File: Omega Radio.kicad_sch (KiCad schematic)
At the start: 14 parts, among them J1 AVR-ISP-6, SW1 Reset, U1 ATmega328P-P

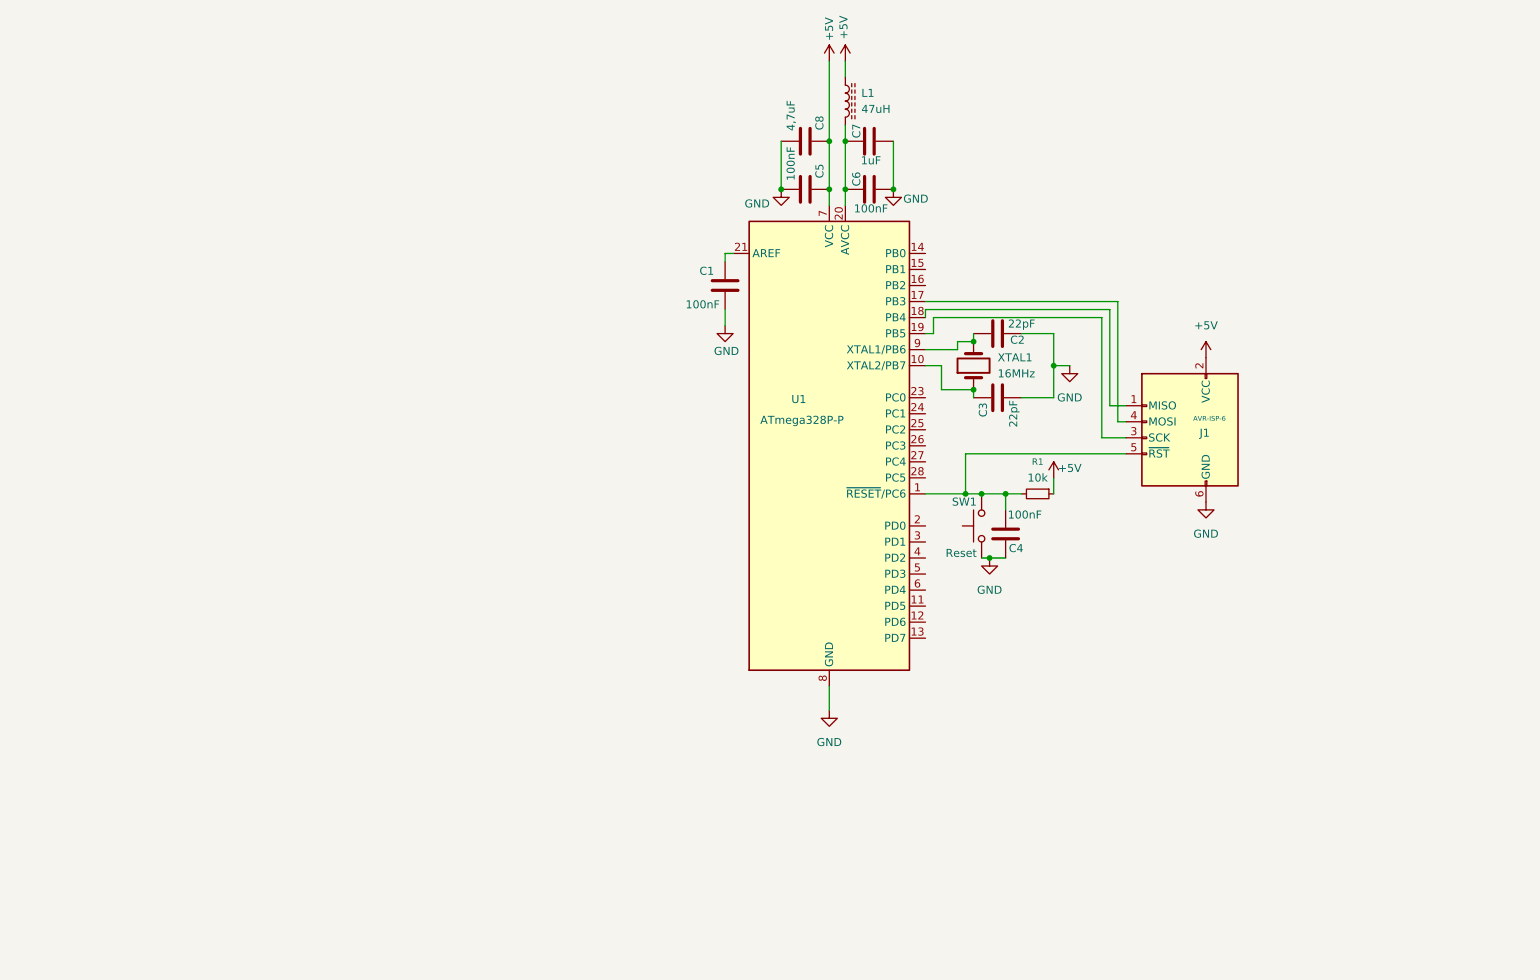
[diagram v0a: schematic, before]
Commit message: Introduction of the regulator to the microprocessor
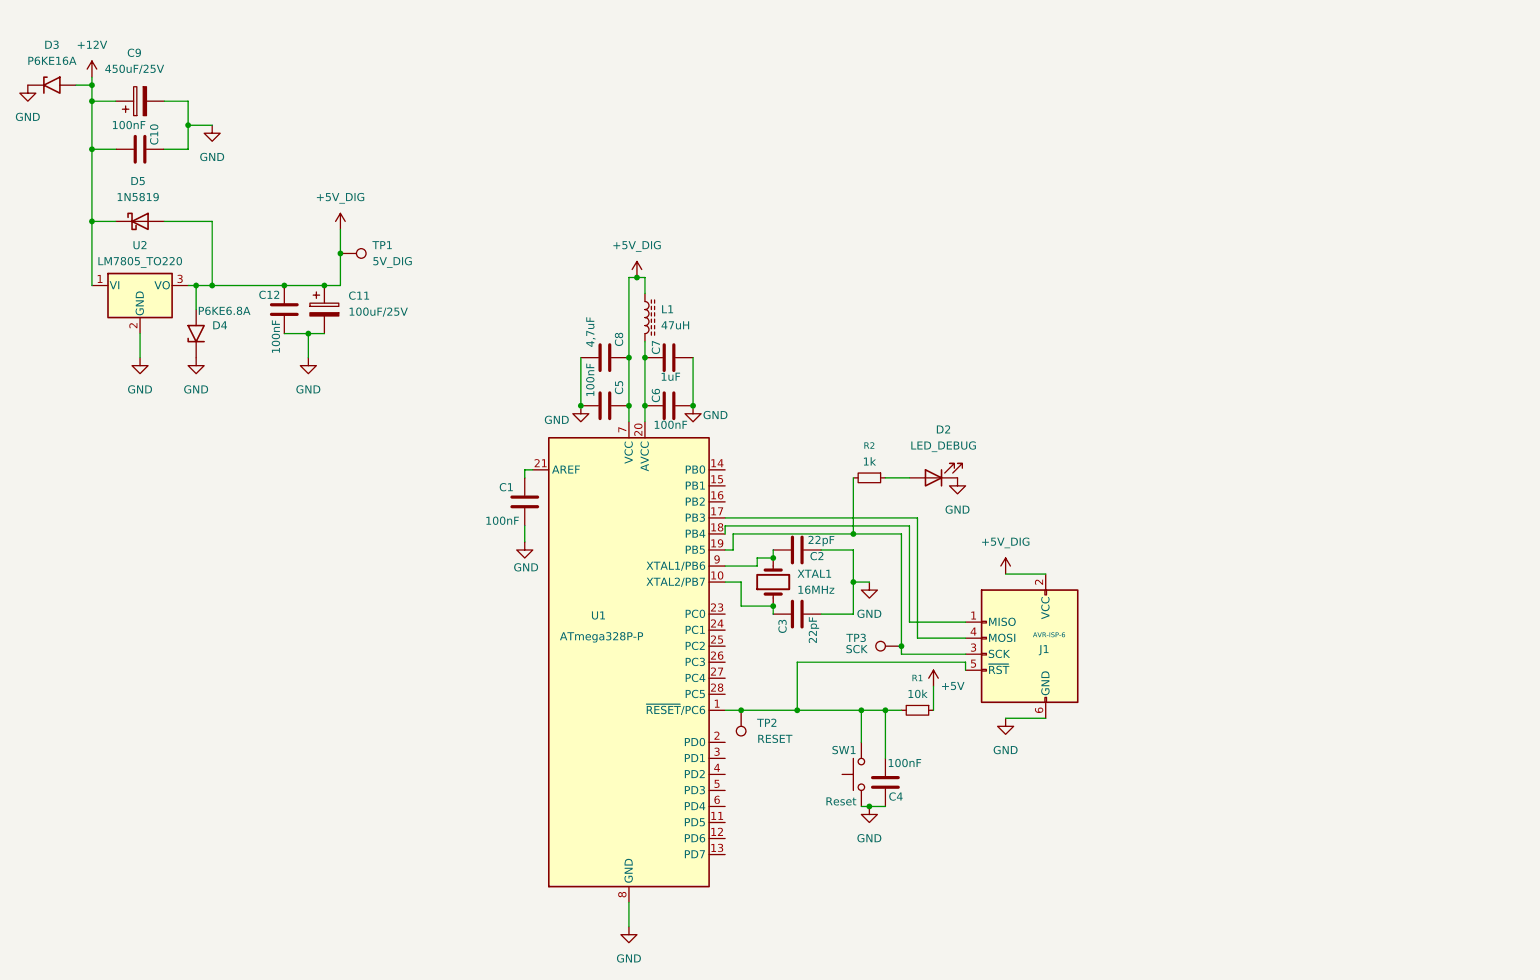
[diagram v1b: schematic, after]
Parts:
- added C10, C12: 100nF, symbol Device:C
- added C11: 100uF/25V, symbol Device:C_Polarized
- added C9: 450uF/25V, symbol Device:C_Polarized
- added D2: LED_DEBUG, symbol Device:LED
- added D3: P6KE16A, Diode_THT:D_P600_R-6_P20.00mm_Horizontal, symbol Diode:5KPxxA
- added D4: P6KE6.8A, Diode_THT:D_P600_R-6_P20.00mm_Horizontal, symbol Diode:5KPxxA
- added D5: 1N5819, Diode_THT:D_DO-41_SOD81_P10.16mm_Horizontal, symbol Diode:1N5819
- added R2: 1k, symbol Device:R_Small
- added TP1: 5V_DIG, symbol Connector:TestPoint
- added TP2: RESET, symbol Connector:TestPoint
- added TP3: SCK, symbol Connector:TestPoint
- added U2: LM7805_TO220, Package_TO_SOT_THT:TO-220-3_Vertical, symbol Regulator_Linear:LM7805_TO220
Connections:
- net +5V: no longer C5.1, C8.1, J1.2 (VCC), L1.1, U1.7 (VCC)
- net GND: now also C10.1, C11.2, C12.2, C9.2, D2.1 (K), D3.1 (A1), D4.1 (A1), U2.2 (GND)
- net at J1.3 (SCK), U1.19 (PB5): now also R2.2, TP3.1
- net at C4.2, J1.5 (~{RST}), R1.2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: now also TP2.1
- new net: D2.2 (A), R2.1
- new net +12V: C10.2, C9.1, D3.2 (A2), D5.1 (K), U2.1 (VI)
- new net +5V_DIG: C11.1, C12.1, C5.1, C8.1, D4.2 (A2), D5.2 (A), J1.2 (VCC), L1.1, TP1.1, U1.7 (VCC), U2.3 (VO)
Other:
- moved on the sheet: C1, C2, C3, C4, C5, C6, C7, C8, J1, L1, R1, SW1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

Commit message: Project paradigm shift
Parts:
- removed C1, C5, C6: 100nF, symbol Device:C
- removed C2, C3: 22pF, symbol Device:C
- removed C7: 1uF, symbol Device:C
- removed C8: 4,7uF, symbol Device:C
- removed D2: LED_DEBUG, symbol Device:LED
- removed D3: P6KE16A, Diode_THT:D_P600_R-6_P20.00mm_Horizontal, symbol Diode:5KPxxA
- removed J1: AVR-ISP-6, symbol Connector:AVR-ISP-6
- removed L1: 47uH, symbol Device:L_Ferrite
- removed R2: 1k, symbol Device:R_Small
- removed U1: ATmega328P-P, Package_DIP:DIP-28_W7.62mm, symbol MCU_Microchip_ATmega:ATmega328P-P
- removed XTAL1: 16MHz, symbol Device:Crystal
- added A1: Arduino_Nano_v3.x, Module:Arduino_Nano, symbol MCU_Module:Arduino_Nano_v3.x
- added C14: 100uF, symbol Device:C_Polarized_Small
- added C15: 10uF, symbol Device:C_Polarized_Small
- added C16, C5, C6: 100nF, symbol Device:C_Small
- added FB1: ≈ 600 Ω @ 100 MHz, symbol Device:FerriteBead_Small
- added FL1: ≥600 Ω @100 MHz,, Inductor_THT:L_CommonMode_PulseElectronics_PH9455x105NL_1, symbol Filter:Choke_CommonMode_PulseElectronics_PH9455x105NL
- added TP4: 5V_DIG2, symbol Connector:TestPoint
- C1: renamed from C9; value 450uF/25V -> 450uF
- C2: renamed from C10; value 100nF -> 330nF
- TP2: value RESET -> GND_LM7895
- TP3: value SCK -> GND_DIG
- renumbered C12 to C3, C11 to C4, C4 to C7, D5 to D1, D4 to D2, U2 to U1
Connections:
- net +5V_DIG: now also D2.1 (A1), FL1.3; no longer D2.2 (A2)
- net GND: now also C2.2, D2.2 (A2), TP2.1, TP3.1, A1.29 (GND), A1.4 (GND), C14.2, C15.2, C16.1, C5.1, C6.2, FL1.1, FL1.4; no longer C2.1, D2.1 (A1)
- net at C7.2, R1.2, SW1.2: now also A1.3 (~{RESET}); no longer TP2.1
- net +12V renamed +12V_SW
- net +12V_SW: now also C2.1; no longer C2.2
- new net: A1.27 (+5V), C15.1, C5.2, FB1.2, TP4.1
- new net: C14.1, C16.2, FB1.1, FL1.2
- new net: A1.18 (AREF), C6.1
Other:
- added sheet Untitled Sheet (io_externos.kicad_sch)
- title: (none) -> Omega Radio
- moved on the sheet: C1, C2, C3, C4, C7, D1, D2, R1, SW1, TP1

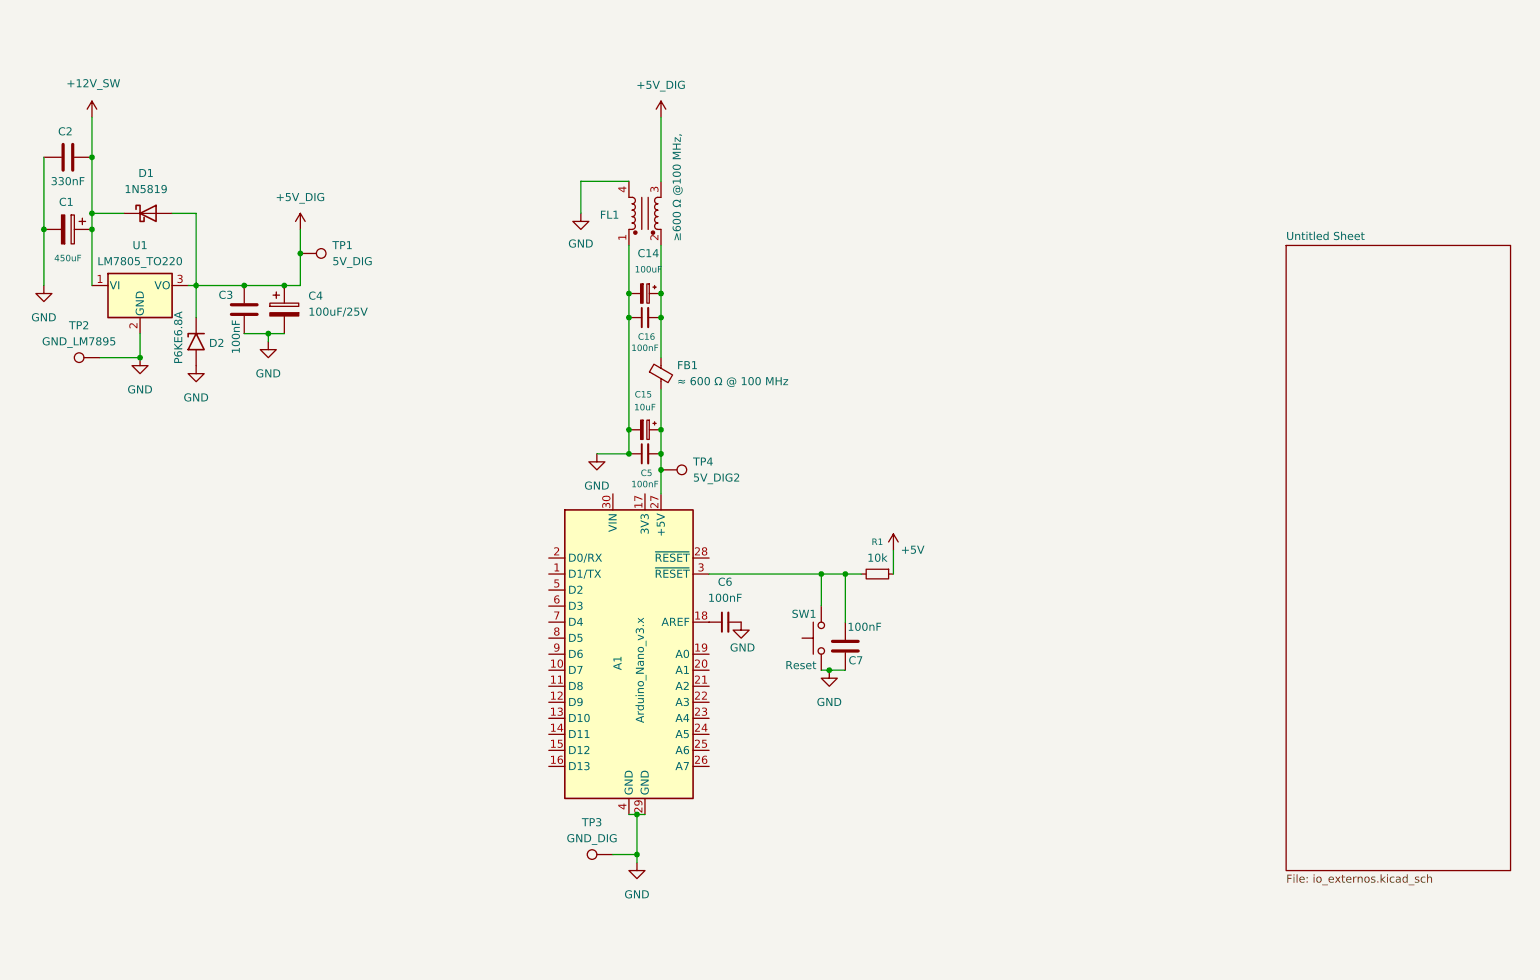
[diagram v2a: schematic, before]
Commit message: starting to draw the driver schematic
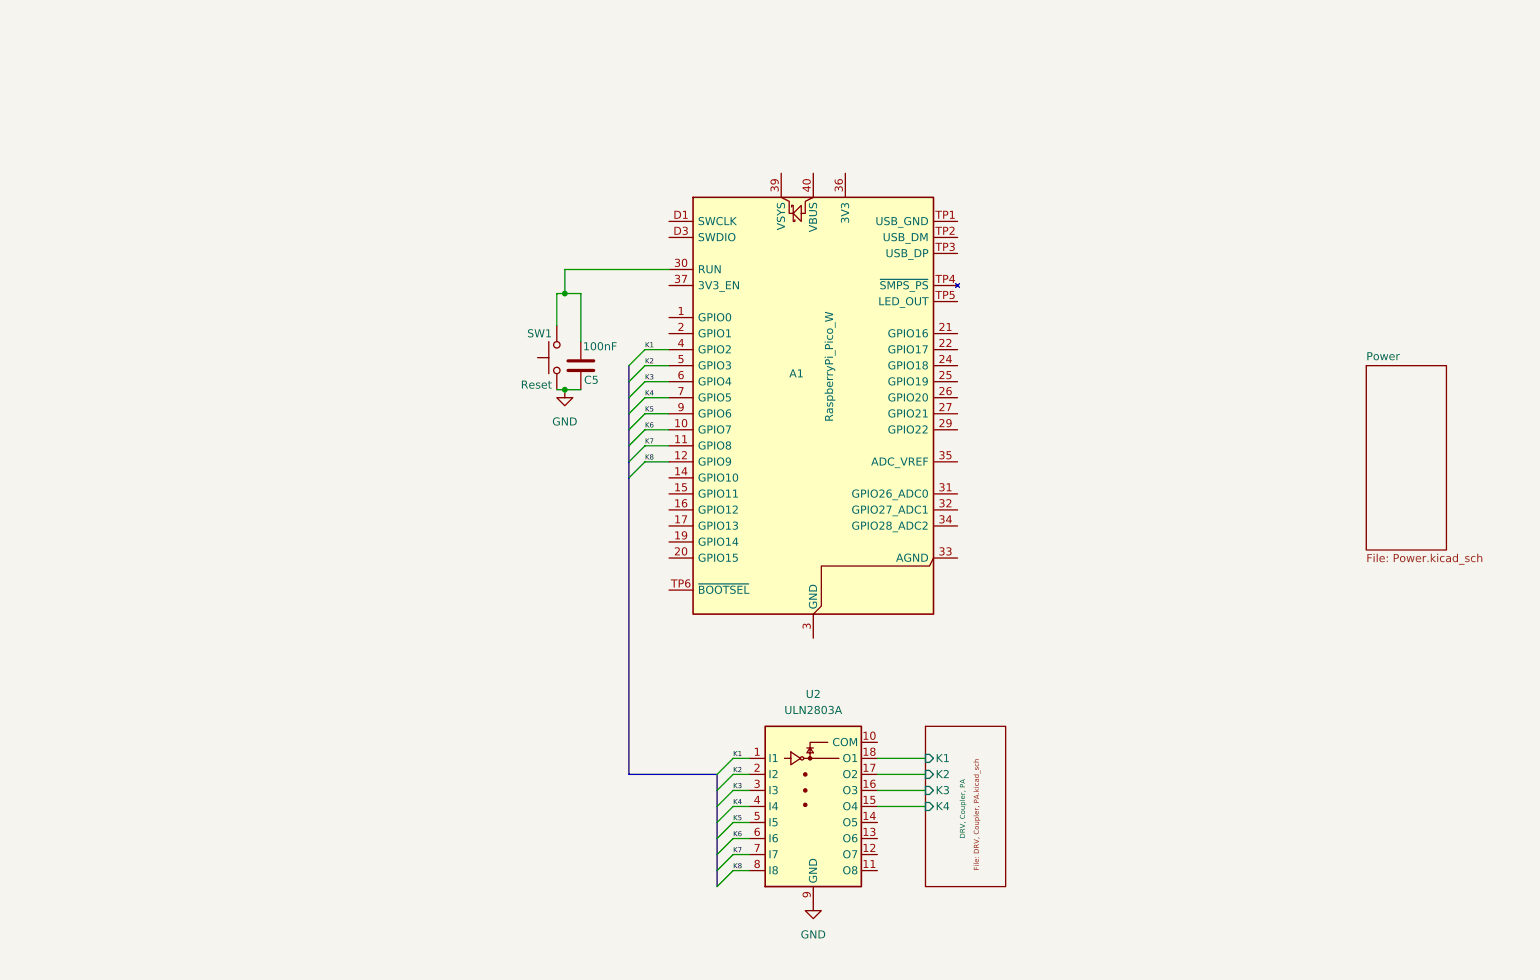
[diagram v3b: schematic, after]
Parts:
- removed A1: Arduino_Nano_v3.x, Module:Arduino_Nano, symbol MCU_Module:Arduino_Nano_v3.x
- removed C1: 450uF, symbol Device:C_Polarized
- removed C14: 100uF, symbol Device:C_Polarized_Small
- removed C15: 10uF, symbol Device:C_Polarized_Small
- removed C16, C5, C6: 100nF, symbol Device:C_Small
- removed C2: 330nF, symbol Device:C
- removed C3: 100nF, symbol Device:C
- removed C4: 100uF/25V, symbol Device:C_Polarized
- removed D1: 1N5819, Diode_THT:D_DO-41_SOD81_P10.16mm_Horizontal, symbol Diode:1N5819
- removed D2: P6KE6.8A, Diode_THT:D_P600_R-6_P20.00mm_Horizontal, symbol Diode:5KPxxA
- removed FB1: ≈ 600 Ω @ 100 MHz, symbol Device:FerriteBead_Small
- removed FL1: ≥600 Ω @100 MHz,, Inductor_THT:L_CommonMode_PulseElectronics_PH9455x105NL_1, symbol Filter:Choke_CommonMode_PulseElectronics_PH9455x105NL
- removed R1: 10k, symbol Device:R_Small
- removed TP1: 5V_DIG, symbol Connector:TestPoint
- removed TP2: GND_LM7895, symbol Connector:TestPoint
- removed TP3: GND_DIG, symbol Connector:TestPoint
- removed TP4: 5V_DIG2, symbol Connector:TestPoint
- removed U1: LM7805_TO220, Package_TO_SOT_THT:TO-220-3_Vertical, symbol Regulator_Linear:LM7805_TO220
- added A1: RaspberryPi_Pico_W, Module:RaspberryPi_Pico_W_SMD, symbol MCU_Module:RaspberryPi_Pico_W_Extensive
- added U2: ULN2803A, symbol Transistor_Array:ULN2803A
- renumbered C7 to C5
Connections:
- net GND: now also U2.9 (GND)
- net at C5.2, SW1.2: now also A1.30 (RUN)
- new net: A1.13 (GND), A1.18 (GND), A1.23 (GND), A1.28 (GND), A1.3 (GND), A1.38 (GND), A1.8 (GND), A1.D2 (GND)
- new net DRV, Coupler, PA/K1: U2.18 (O1)
- new net DRV, Coupler, PA/K2: U2.17 (O2)
- new net DRV, Coupler, PA/K3: U2.16 (O3)
- new net DRV, Coupler, PA/K4: U2.15 (O4)
- new net K1: A1.4 (GPIO2), U2.1 (I1)
- new net K2: A1.5 (GPIO3), U2.2 (I2)
- new net K3: A1.6 (GPIO4), U2.3 (I3)
- new net K4: A1.7 (GPIO5), U2.4 (I4)
- new net K5: A1.9 (GPIO6), U2.5 (I5)
- new net K6: A1.10 (GPIO7), U2.6 (I6)
- new net K7: A1.11 (GPIO8), U2.7 (I7)
- new net K8: A1.12 (GPIO9), U2.8 (I8)
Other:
- sheet Untitled Sheet renamed DRV, Coupler, PA
- added sheet Power (Power.kicad_sch)
- sheet DRV, Coupler, PA: file io_externos.kicad_sch -> DRV, Coupler, PA.kicad_sch
- sheet DRV, Coupler, PA ports: added K1, K2, K3, K4; removed none
- moved on the sheet: C5, SW1

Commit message: Driver done.
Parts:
- renumbered C5 to C1, U2 to U1
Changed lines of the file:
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@@
 		(dnp no)
 		(fields_autoplaced yes)
-		(property "Reference" "#PWR037"
+		(property "Reference" "#PWR02"
 			(at 143.51 160.02 0)
 			(effects
@@
 			(project "Omega Radio"
 				(path "/3468ce30-82a7-4087-a7ac-02063723d842"
-					(reference "#PWR037")
+					(reference "#PWR02")
 					(unit 1)
 				)
@@
 		(on_board yes)
 		(dnp no)
-		(property "Reference" "C5"
+		(property "Reference" "C1"
 			(at 107.188 70.866 0)
 			(do_not_autoplace yes)
@@
 			(project "Omega Radio"
 				(path "/3468ce30-82a7-4087-a7ac-02063723d842"
-					(reference "C5")
+					(reference "C1")
 					(unit 1)
 				)
@@
 		(dnp no)
 		(fields_autoplaced yes)
-		(property "Reference" "#PWR07"
+		(property "Reference" "#PWR01"
 			(at 104.14 78.74 0)
 			(effects
@@
 			(project ""
 				(path "/3468ce30-82a7-4087-a7ac-02063723d842"
-					(reference "#PWR07")
+					(reference "#PWR01")
 					(unit 1)
 				)
@@
 		(dnp no)
 		(fields_autoplaced yes)
-		(property "Reference" "U2"
+		(property "Reference" "U1"
 			(at 143.51 120.65 0)
 			(effects
@@
 			(project "Omega Radio"
 				(path "/3468ce30-82a7-4087-a7ac-02063723d842"
-					(reference "U2")
+					(reference "U1")
 					(unit 1)
 				)

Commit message: huge modification of the project.
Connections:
- net DRV, Coupler, PA/K1: no longer names the net of U1.18 (O1)
- net DRV, Coupler, PA/K2: no longer names the net of U1.17 (O2)
- net DRV, Coupler, PA/K3: no longer names the net of U1.16 (O3)
- net DRV, Coupler, PA/K4: no longer names the net of U1.15 (O4)
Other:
- added sheet RF, IF (rf_if.kicad_sch)
- sheet DRV, Coupler, PA ports: added none; removed K1, K2, K3, K4
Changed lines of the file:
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@@
 	(title_block
 		(title "Omega Radio")
-		(comment 1 "Regulator, Microprocessor, Relays ")
+		(comment 1 "Logical ")
 	)
 	(junction
@@
 	(wire
 		(pts
-			(xy 153.67 130.81) (xy 161.29 130.81)
-		)
-		(stroke
-			(width 0)
-			(type default)
-		)
-	)
-	(wire
-		(pts
 			(xy 116.84 73.66) (xy 120.65 73.66)
 		)
@@
 	(wire
 		(pts
-			(xy 153.67 135.89) (xy 161.29 135.89)
-		)
-		(stroke
-			(width 0)
-			(type default)
-		)
-	)
-	(wire
-		(pts
 			(xy 102.87 72.39) (xy 104.14 72.39)
 		)
@@
 		)
 	)
-	(wire
-		(pts
-			(xy 153.67 133.35) (xy 161.29 133.35)
-		)
-		(stroke
-			(width 0)
-			(type default)
-		)
-	)
 	(bus
 		(pts
@@
 		(pts
 			(xy 116.84 78.74) (xy 120.65 78.74)
-		)
-		(stroke
-			(width 0)
-			(type default)
-		)
-	)
-	(wire
-		(pts
-			(xy 153.67 138.43) (xy 161.29 138.43)
 		)
 		(stroke
@@
 			)
 		)
-		(pin "K1" input
-			(at 161.29 130.81 180)
-			(effects
-				(font
-					(size 1.27 1.27)
-				)
-				(justify left)
-			)
-		)
-		(pin "K2" input
-			(at 161.29 133.35 180)
-			(effects
-				(font
-					(size 1.27 1.27)
-				)
-				(justify left)
-			)
-		)
-		(pin "K3" input
-			(at 161.29 135.89 180)
-			(effects
-				(font
-					(size 1.27 1.27)
-				)
-				(justify left)
-			)
-		)
-		(pin "K4" input
-			(at 161.29 138.43 180)
-			(effects
-				(font
-					(size 1.27 1.27)
-				)
-				(justify left)
-			)
-		)
 		(instances
 			(project "Omega Radio"
@@
 				)
 			)
+		)
+	)
+	(sheet
+		(at 231 109)
+		(size 13 20)
+		(exclude_from_sim no)
+		(in_bom yes)
+		(on_board yes)
+		(dnp no)
+		(fields_autoplaced yes)
+		(stroke
+			(width 0.1524)
+			(type solid)
+		)
+		(fill
+			(color 0 0 0 0.0000)
+		)
+		(property "Sheetname" "RF, IF"
+			(at 231 108.2884 0)
+			(effects
+				(font
+					(size 1.27 1.27)
+				)
+				(justify left bottom)
+			)
+		)
+		(property "Sheetfile" "rf_if.kicad_sch"
+			(at 231 129.5846 0)
+			(effects
+				(font
+					(size 1.27 1.27)
+				)
+				(justify left top)
+			)
+		)
+		(instances
+			(project "Omega Radio"
+				(path "/3468ce30-82a7-4087-a7ac-02063723d842"
+					(page "4")
+				)
+			)

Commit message: PA reformulation
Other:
- sheet DRV, Coupler, PA renamed DRV, PA
- sheet DRV, PA: file DRV, Coupler, PA.kicad_sch -> DRV, PA.kicad_sch
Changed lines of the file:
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@@
 			(color 0 0 0 0.0000)
 		)
-		(property "Sheetname" "DRV, Coupler, PA"
+		(property "Sheetname" "DRV, PA"
 			(at 167.64 143.51 90)
 			(effects
@@
 			)
 		)
-		(property "Sheetfile" "DRV, Coupler, PA.kicad_sch"
+		(property "Sheetfile" "DRV, PA.kicad_sch"
 			(at 168.91 148.59 90)
 			(effects

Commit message: LPF work
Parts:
- removed A1: RaspberryPi_Pico_W, Module:RaspberryPi_Pico_W_SMD, symbol MCU_Module:RaspberryPi_Pico_W_Extensive
- removed C1: 100nF, symbol Device:C
- removed SW1: Reset, symbol Switch:SW_Push
- removed U1: ULN2803A, symbol Transistor_Array:ULN2803A
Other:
- added sheet Control (control.kicad_sch)
- added sheet LPF(PA cont) (LPF(PA cont).kicad_sch)
